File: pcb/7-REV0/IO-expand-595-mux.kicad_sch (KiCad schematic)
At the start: 75 parts, among them Q300 BC2301T 2.8A, Q301 BC2301T 2.8A, Q302 BC2301T 2.8A, Q303 BC2301T 2.8A, Q304 BC2301T 2.8A, Q305 BC2301T 2.8A, Q306 BC2301T 2.8A, Q307 BC2301T 2.8A, U2 74LVC8T245BQ, U402 CD4067, U404 LMV321, U503 74HCT245BQ, U504 GS324MT/TR, U505 GS324MT/TR, U506 LMV321

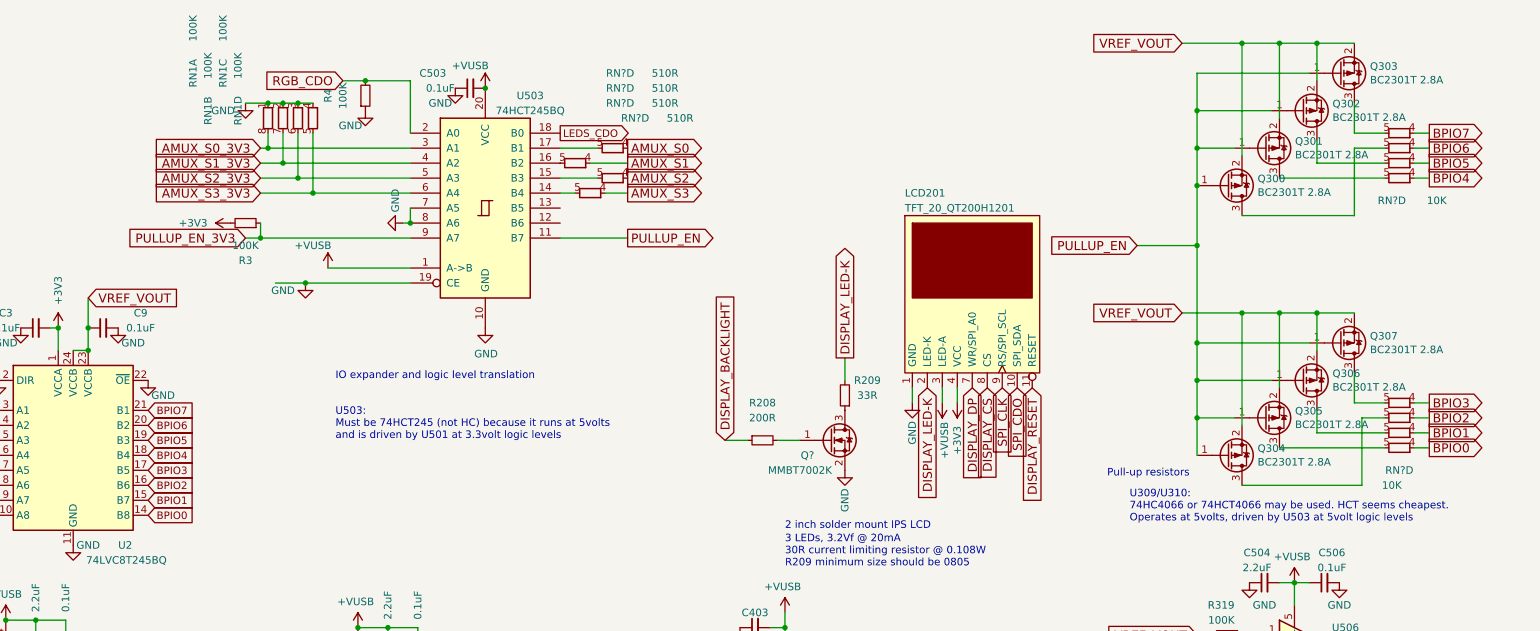
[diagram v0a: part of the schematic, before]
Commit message: remove old pullups, remove 1M pull-down. Add footprints and updated PCB.
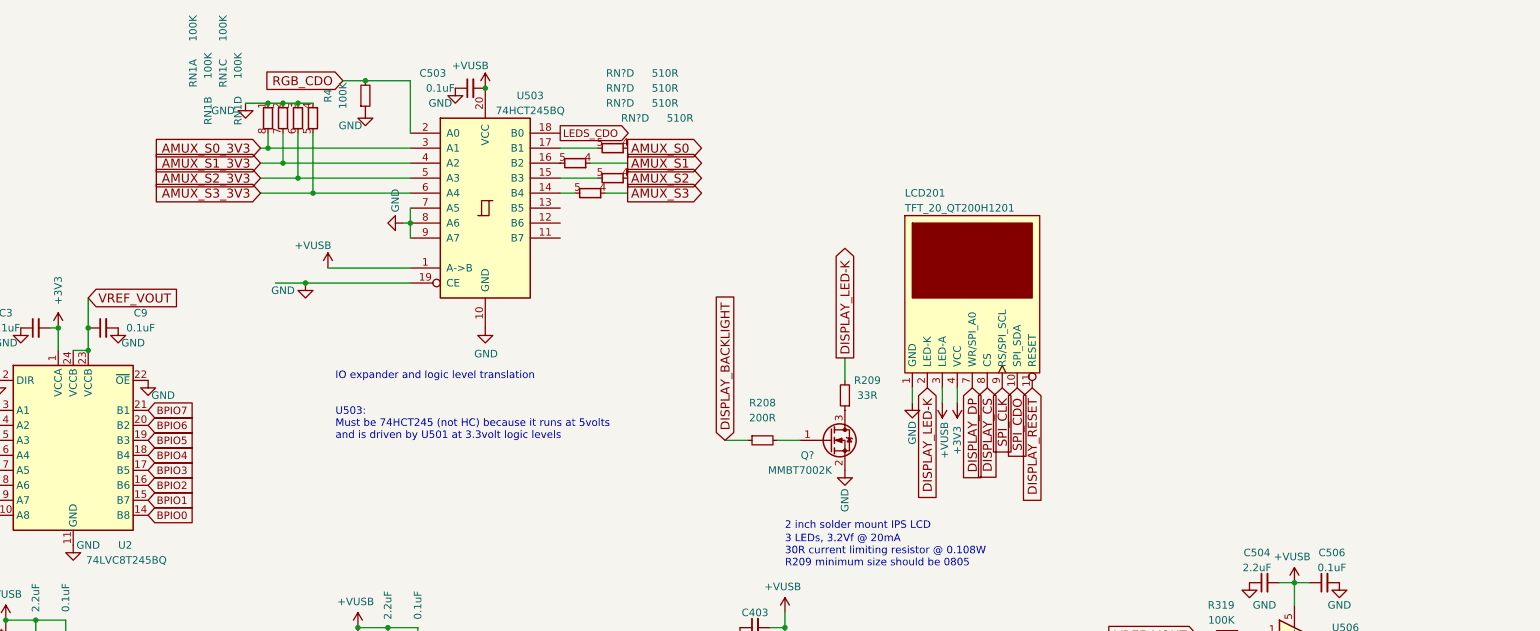
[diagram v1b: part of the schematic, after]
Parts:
- removed Q300, Q301, Q302, Q303, Q304, Q305, Q306, Q307: BC2301T 2.8A, Package_TO_SOT_SMD:SOT-523, symbol Transistor_FET:BSS84
- removed R3: 100K, Resistor_SMD:R_0402_1005Metric, symbol Device:R_Small
- removed RN? (x8): 10K, Resistor_SMD:R_Array_Convex_4x0402, symbol dp-rarray:R_Array
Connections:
- net PULLUP_EN_3V3 is gone; now on net GND: U503.9 (A7)
- net PULLUP_EN: no longer names the net of U503.11 (B7)
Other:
- note removed: "Pull-up resistors"
- note removed: "U309/U310: 74HC4066 or 74HCT4066 may be used. HCT seems cheapest. Operates at 5volts, driven by U503 at 5volt logic levels"

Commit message: partial move to dfn/qfn
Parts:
- removed C405, C504: 2.2uF, Capacitor_SMD:C_0402_1005Metric, symbol Device:C_Small
- removed U504, U505: GS324MT/TR, Package_SO:TSSOP-14_4.4x5mm_P0.65mm, symbol Amplifier_Operational:LM324
- added U10, U11, U12, U13, U9: LM358_DFN, Package_DFN_QFN:DFN-8-1EP_2x2mm_P0.5mm_EP1.05x1.75mm, symbol Amplifier_Operational:LM358_DFN
- C507, C509: value 2.2uF -> 0.1uF
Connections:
- net +VUSB: now also U10.8 (V+), U11.8 (V+), U12.8 (V+), U9.8 (V+)
- net GND: now also U10.4 (V-), U11.4 (V-), U12.4 (V-), U9.4 (V-)
- net MUX_BPIO0: now also U9.6 (-), U9.7
- net MUX_BPIO1: now also U9.1, U9.2 (-)
- net MUX_BPIO2: now also U10.1, U10.2 (-)
- net MUX_BPIO3: now also U10.6 (-), U10.7
- net MUX_BPIO4: now also U11.6 (-), U11.7
- net MUX_BPIO5: now also U11.1, U11.2 (-)
- net MUX_BPIO6: now also U12.1, U12.2 (-)
- net MUX_BPIO7: now also U12.6 (-), U12.7
- net at D503.1, RN?.4 (R1.1): now also U10.5 (+)
- net at D501.1, RN?.4 (R1.1): now also U12.5 (+)
- net at D501.2, RN?.4 (R1.1): now also U12.3 (+)
- net at D503.2, RN?.4 (R1.1): now also U10.3 (+)
- net at D502.1, RN?.4 (R1.1): now also U11.3 (+)
- net at D502.2, RN?.4 (R1.1): now also U11.5 (+)
- net at D504.1, RN?.4 (R1.1): now also U9.3 (+)
- net at D504.2, RN?.4 (R1.1): now also U9.5 (+)
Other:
- moved on the sheet: C3, C503, C507, C508, C509, C510, C9, D501, D502, D503, D504, LCD201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

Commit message: minor updates to collaborative board redesign
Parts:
- removed C406, C506: 0.1uF, Capacitor_SMD:C_0402_1005Metric, symbol Device:C_Small
- removed RN? (x4): 510R, Resistor_SMD:R_Array_Convex_4x0402, symbol dp-rarray:R_Array
- removed U404, U506: LMV321, Package_TO_SOT_SMD:SOT-23-5, symbol Comparator:LMV331
- added C20: 0.1uF, Capacitor_SMD:C_0402_1005Metric, symbol Device:C_Small
- added R3, R5: 510R, Resistor_SMD:R_0402_1005Metric, symbol Device:R_Small
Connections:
- net +VUSB: now also U13.8 (V+), C20.2
- net GND: now also U13.4 (V-), C20.1
- net MUX_VREF_VOUT: now also U13.1, U13.2 (-), R3.2
- net VREG_OUT: now also R5.2
- net at R406.1: now also U13.6 (-), U13.7
- net at U402.1 (COM): now also U13.5 (+)
- net at U402.21 (I10): now also R5.1
- net at U402.22 (I9): now also R3.1
- net at D500.1, R319.1: now also U13.3 (+)
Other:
- moved on the sheet: C403, C503, D500, R319, R320, R4, R406, R407, RN1A, RN1B, RN1C, RN1D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
